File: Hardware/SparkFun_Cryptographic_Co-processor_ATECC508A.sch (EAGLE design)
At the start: 22 parts, among them J1 QWIIC, J2 QWIIC, J3 PTH, U1 ATECC508A

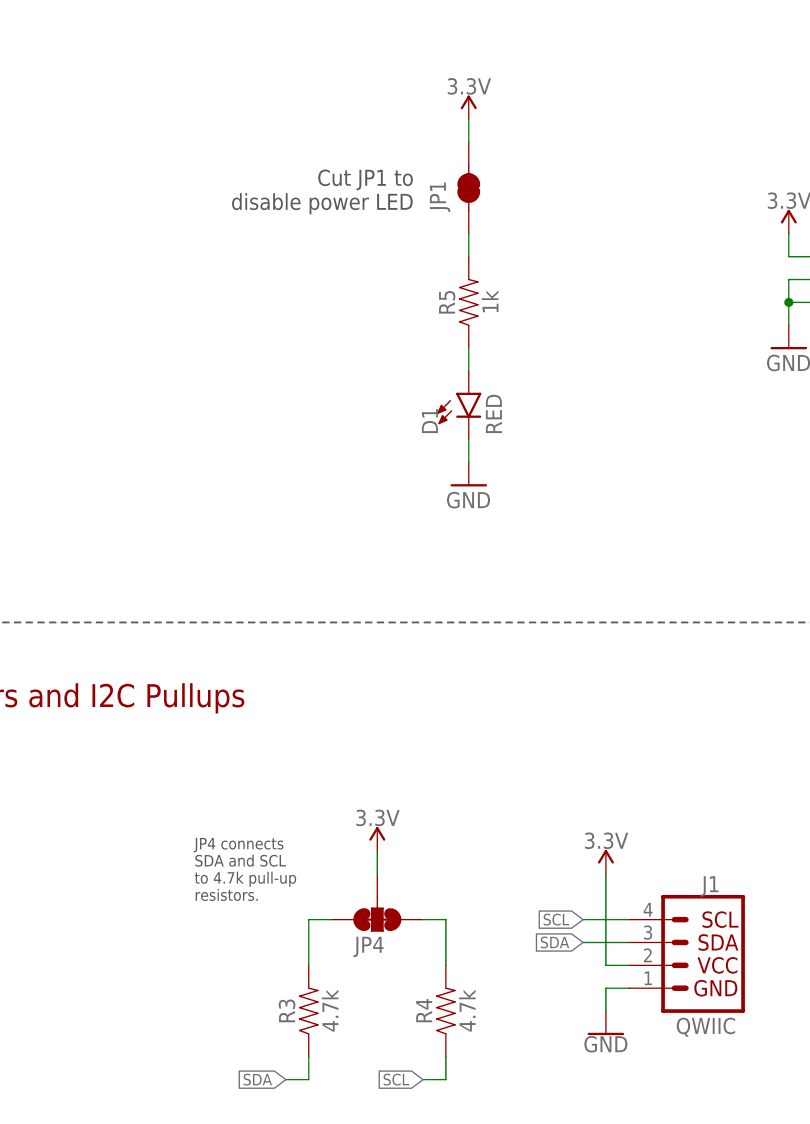
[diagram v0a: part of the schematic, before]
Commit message: silk on jumpers, rotate I2C jumper label, changed name on symbols to match
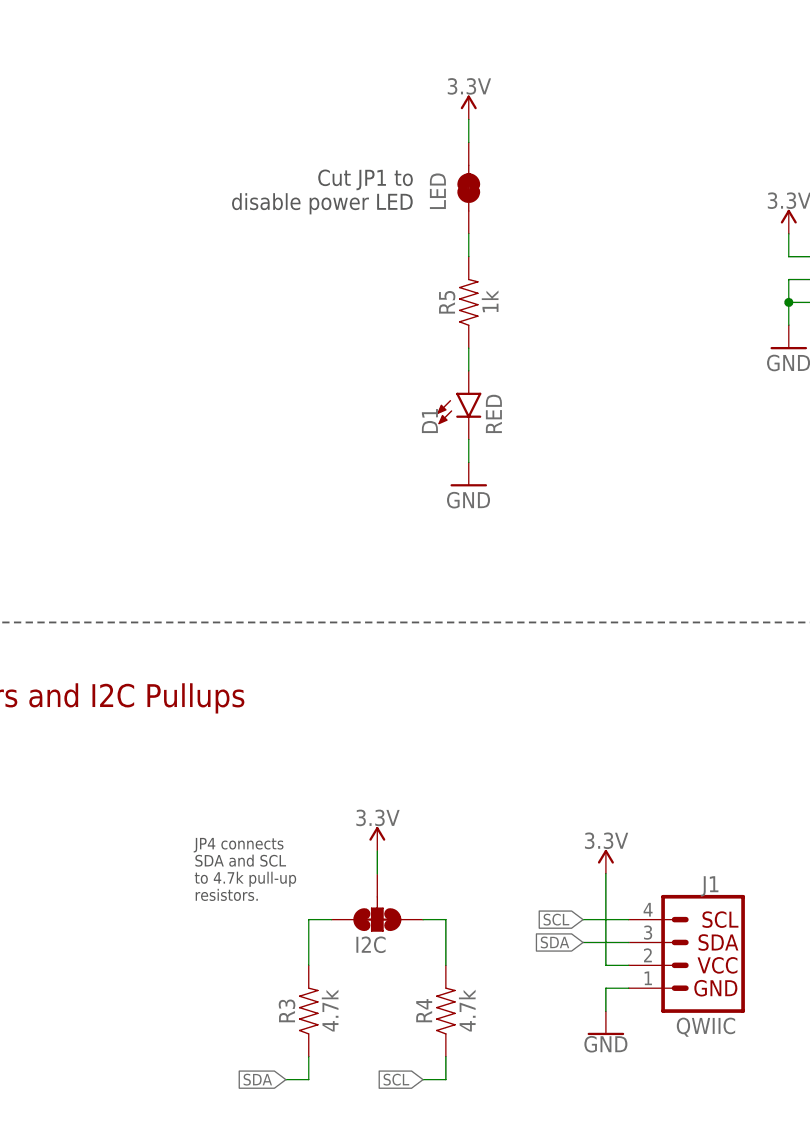
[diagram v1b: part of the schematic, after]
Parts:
- removed JP1: JUMPER-SMT_2_NC_TRACE_NO-SILK, SparkFun-Jumpers:JUMPER-SMT_2_NC_TRACE_NO-SILK
- removed JP4: JUMPER-SMT_3_2-NC_TRACE_NO-SILK, SparkFun-Jumpers:JUMPER-SMT_3_2-NC_TRACE_NO-SILK
- added I2C: JUMPER-SMT_3_2-NC_TRACE_SILK, SparkFun-Jumpers:JUMPER-SMT_3_2-NC_TRACE_SILK
- added LED: JUMPER-SMT_2_NC_TRACE_SILK, SparkFun-Jumpers:JUMPER-SMT_2_NC_TRACE_SILK
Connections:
- net 3.3V: now also I2C.2, LED.2; no longer JP1.2, JP4.2
- net N$4: now also I2C.3; no longer JP4.3
- net N$5: now also I2C.1; no longer JP4.1
- net N$7: now also LED.1; no longer JP1.1

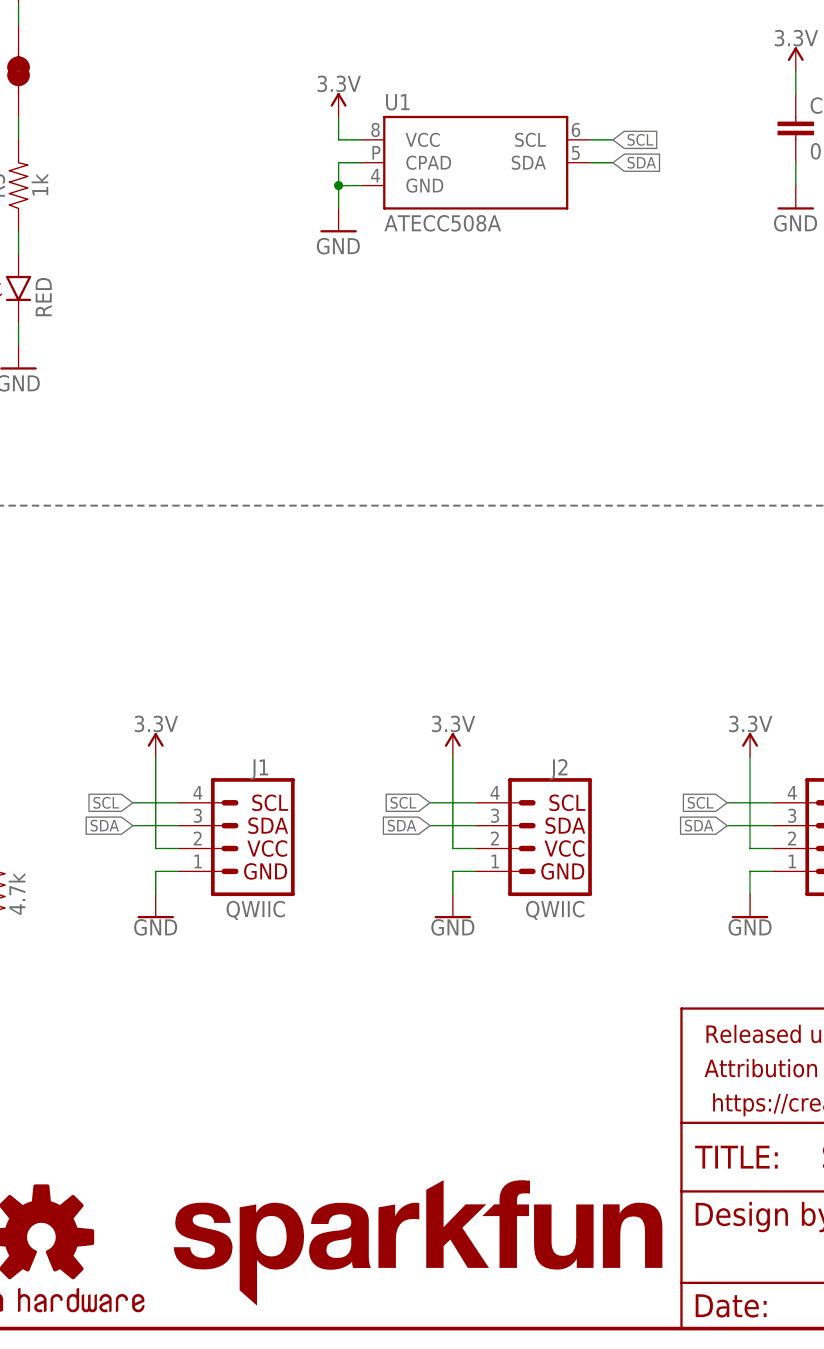
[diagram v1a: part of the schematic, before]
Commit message: Design review changes - silk, sch, prod id - ready for reds
-added sweet key graphic
-added default I2C address to sch
-added PROD ID to part in library. (note, still need to migrate to official libraries when this goes live).
-added NC pin to symbol/dev for IC.
-nudges a via and some traces to line up with key graphic hole
-rotated LED label to match others' orientation.
-swapped jumper packages to include silk outlines
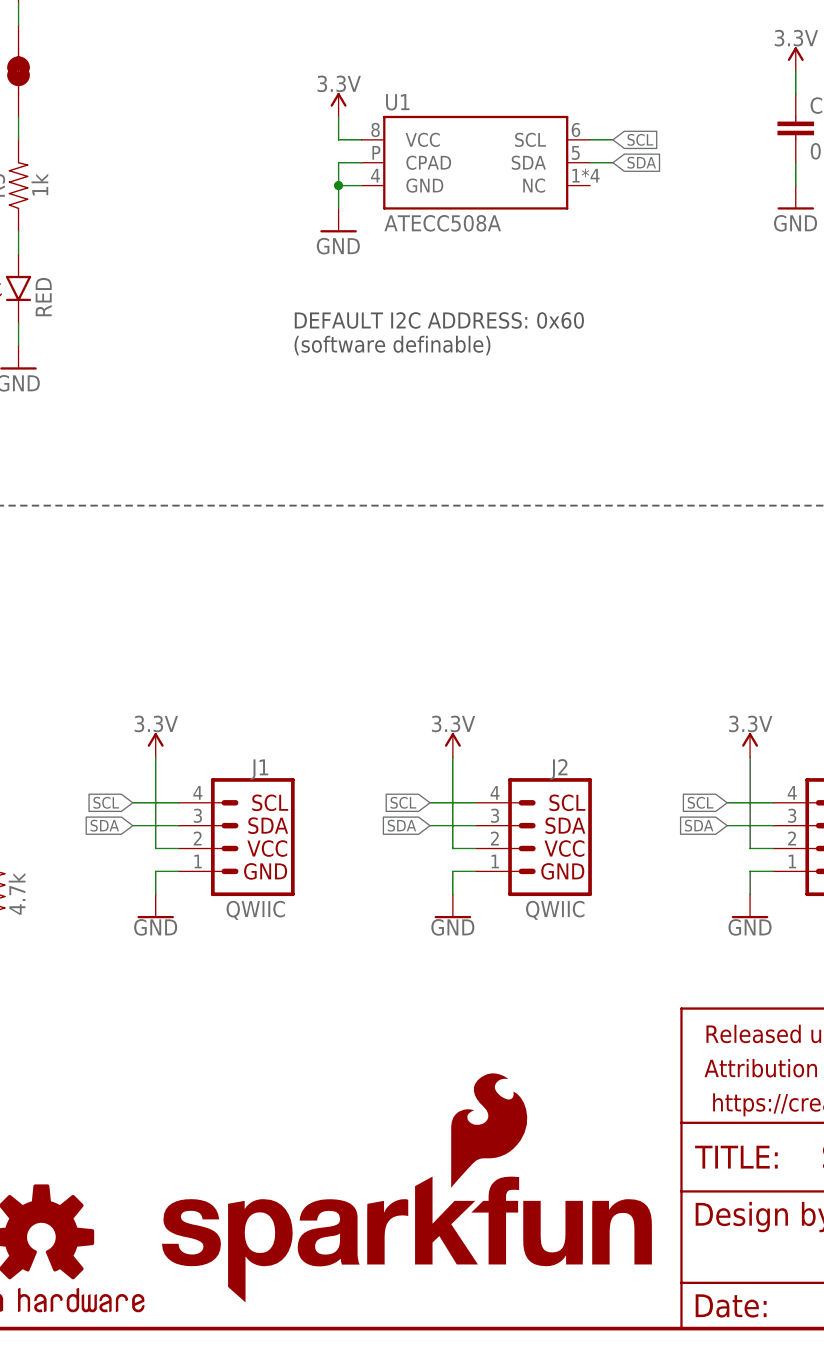
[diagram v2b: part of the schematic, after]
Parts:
- LOGO1: value SFE_LOGO_NAME.1_INCH -> SFE_LOGO_NAME_FLAME.1_INCH; device SparkFun-Aesthetics:SFE_LOGO_NAME.1_INCH -> SparkFun-Aesthetics:SFE_LOGO_NAME_FLAME.1_INCH
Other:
- note added: "DEFAULT I2C ADDRESS: 0x60 (software definable)"
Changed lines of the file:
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@@
 <part name="SUPPLY4" library="SparkFun-PowerSymbols" deviceset="3.3V" device=""/>
 <part name="J2" library="SparkFun-Connectors" deviceset="I2C_STANDARD" device="QWIIC" value="QWIIC"/>
-<part name="LOGO1" library="SparkFun-Aesthetics" deviceset="SFE_LOGO_NAME" device=".1_INCH"/>
+<part name="LOGO1" library="SparkFun-Aesthetics" deviceset="SFE_LOGO_NAME_FLAME" device=".1_INCH"/>
 <part name="FD3" library="SparkFun-Aesthetics" deviceset="FIDUCIAL" device="1X2"/>
 <part name="FD4" library="SparkFun-Aesthetics" deviceset="FIDUCIAL" device="1X2"/>
@@
 <text x="67.564" y="141.732" size="1.778" layer="97" font="vector" align="top-right">Cut JP1 to
 disable power LED</text>
+<text x="104.14" y="108.458" size="1.778" layer="97" font="vector">DEFAULT I2C ADDRESS: 0x60
+(software definable)</text>
 </plain>
 <instances>
